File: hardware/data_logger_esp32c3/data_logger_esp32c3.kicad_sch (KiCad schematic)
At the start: 5 parts, among them U1 ESP32-C3-MINI-1

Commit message: remove backups
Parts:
- added J?: USB_C_Receptacle_USB2.0, symbol Connector:USB_C_Receptacle_USB2.0
- added R? (x2): 5.1k, symbol Device:R_Small
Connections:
- net GND: now also J?.A1 (GND), J?.A12 (GND), J?.B1 (GND), J?.B12 (GND), J?.S1 (SHIELD), R?.1, R?.2
- net D-: now reaches U1.26 (GPIO18/USB_D-)
- net D-: now also J?.A7 (D-), J?.B7 (D-)
- net D+: now reaches U1.27 (GPIO19/USB_D+)
- net D+: now also J?.A6 (D+), J?.B6 (D+)
- new net: J?.B5 (CC2), R?.1
- new net: J?.A5 (CC1), R?.2
- new net VBUS: J?.A4 (VBUS), J?.A9 (VBUS), J?.B4 (VBUS), J?.B9 (VBUS)
- no-connect marks 0 -> 2
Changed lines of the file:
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@@
   (junction (at 97.79 114.3) (diameter 0) (color 0 0 0 0)
   )
+  (junction (at 30.48 167.64) (diameter 0) (color 0 0 0 0)
+  )
+  (no_connect (at 53.34 157.48))
+  (no_connect (at 53.34 160.02))
+  (wire (pts (xy 53.34 137.16) (xy 74.93 137.16))
+    (stroke (width 0) (type default) (color 0 0 0 0))
+  )
   (wire (pts (xy 92.71 114.3) (xy 97.79 114.3))
     (stroke (width 0) (type default) (color 0 0 0 0))
   )
+  (wire (pts (xy 53.34 142.24) (xy 53.34 144.78))
+    (stroke (width 0) (type default) (color 0 0 0 0))
+  )
   (wire (pts (xy 92.71 109.22) (xy 102.87 109.22))
     (stroke (width 0) (type default) (color 0 0 0 0))
@@
     (stroke (width 0) (type default) (color 0 0 0 0))
   )
+  (wire (pts (xy 53.34 147.32) (xy 53.34 149.86))
+    (stroke (width 0) (type default) (color 0 0 0 0))
+  )
+  (wire (pts (xy 30.48 167.64) (xy 38.1 167.64))
+    (stroke (width 0) (type default) (color 0 0 0 0))
+  )
+  (wire (pts (xy 53.34 134.62) (xy 82.55 134.62))
+    (stroke (width 0) (type default) (color 0 0 0 0))
+  )
   (wire (pts (xy 102.87 109.22) (xy 107.95 109.22))
     (stroke (width 0) (type default) (color 0 0 0 0))
@@
   (wire (pts (xy 97.79 114.3) (xy 102.87 114.3))
     (stroke (width 0) (type default) (color 0 0 0 0))
+  )
+  (global_label "D-" (shape input) (at 53.34 142.24 0) (fields_autoplaced)
+    (effects (font (size 1.27 1.27)) (justify left))
+    (property "Intersheet References" "${INTERSHEET_REFS}" (id 0) (at 58.5955 142.1606 0)
+      (effects (font (size 1.27 1.27)) (justify left) hide)
+    )
+  )
+  (global_label "D-" (shape input) (at 107.95 88.9 180) (fields_autoplaced)
+    (effects (font (size 1.27 1.27)) (justify right))
+    (property "Intersheet References" "${INTERSHEET_REFS}" (id 0) (at 102.6945 88.9794 0)
+      (effects (font (size 1.27 1.27)) (justify right) hide)
+    )
+  )
+  (global_label "D+" (shape input) (at 107.95 91.44 180) (fields_autoplaced)
+    (effects (font (size 1.27 1.27)) (justify right))
+    (property "Intersheet References" "${INTERSHEET_REFS}" (id 0) (at 102.6945 91.5194 0)
+      (effects (font (size 1.27 1.27)) (justify right) hide)
+    )
+  )
+  (global_label "D+" (shape input) (at 53.34 147.32 0) (fields_autoplaced)
+    (effects (font (size 1.27 1.27)) (justify left))
+    (property "Intersheet References" "${INTERSHEET_REFS}" (id 0) (at 58.5955 147.2406 0)
+      (effects (font (size 1.27 1.27)) (justify left) hide)
+    )
+  )
+  (symbol (lib_id "power:GND") (at 74.93 142.24 0) (unit 1)
+    (in_bom yes) (on_board yes) (fields_autoplaced)
+    (property "Reference" "#PWR?" (id 0) (at 74.93 148.59 0)
+      (effects (font (size 1.27 1.27)) hide)
+    )
+    (property "Value" "GND" (id 1) (at 74.93 147.32 0))
+    (property "Footprint" "" (id 2) (at 74.93 142.24 0)
+      (effects (font (size 1.27 1.27)) hide)
+    )
+    (property "Datasheet" "" (id 3) (at 74.93 142.24 0)
+      (effects (font (size 1.27 1.27)) hide)
+    )
+    (pin "1")
   )
   (symbol (lib_id "power:GND") (at 83.82 58.42 0) (unit 1)
@@
     )
     (property "Datasheet" "" (id 3) (at 83.82 58.42 0)
+      (effects (font (size 1.27 1.27)) hide)
+    )
+    (pin "1")
+  )
+  (symbol (lib_id "Device:R_Small") (at 74.93 139.7 0) (unit 1)
+    (in_bom yes) (on_board yes) (fields_autoplaced)
+    (property "Reference" "R?" (id 0) (at 77.47 138.4299 0)
+      (effects (font (size 1.27 1.27)) (justify left))
+    )
+    (property "Value" "5.1k" (id 1) (at 77.47 140.9699 0)
+      (effects (font (size 1.27 1.27)) (justify left))
+    )
+    (property "Footprint" "" (id 2) (at 74.93 139.7 0)
+      (effects (font (size 1.27 1.27)) hide)
+    )
+    (property "Datasheet" "~" (id 3) (at 74.93 139.7 0)
+      (effects (font (size 1.27 1.27)) hide)
+    )
+    (pin "1")
+    (pin "2")
+  )
+  (symbol (lib_id "Connector:USB_C_Receptacle_USB2.0") (at 38.1 144.78 0) (unit 1)
+    (in_bom yes) (on_board yes) (fields_autoplaced)
+    (property "Reference" "J?" (id 0) (at 38.1 121.92 0))
+    (property "Value" "USB_C_Receptacle_USB2.0" (id 1) (at 38.1 124.46 0))
+    (property "Footprint" "" (id 2) (at 41.91 144.78 0)
+      (effects (font (size 1.27 1.27)) hide)
+    )
+    (property "Datasheet" "https://www.usb.org/sites/default/files/documents/usb_type-c.zip" (id 3) (at 41.91 144.78 0)
+      (effects (font (size 1.27 1.27)) hide)
+    )
+    (pin "A1")
+    (pin "A12")
+    (pin "A4")
+    (pin "A5")
+    (pin "A6")
+    (pin "A7")
+    (pin "A8")
+    (pin "A9")
+    (pin "B1")
+    (pin "B12")
+    (pin "B4")
+    (pin "B5")
+    (pin "B6")
+    (pin "B7")
+    (pin "B8")
+    (pin "B9")
+    (pin "S1")
+  )
+  (symbol (lib_id "power:GND") (at 82.55 139.7 0) (unit 1)
+    (in_bom yes) (on_board yes) (fields_autoplaced)
+    (property "Reference" "#PWR?" (id 0) (at 82.55 146.05 0)
+      (effects (font (size 1.27 1.27)) hide)
+    )
+    (property "Value" "GND" (id 1) (at 82.55 144.78 0))
+    (property "Footprint" "" (id 2) (at 82.55 139.7 0)
+      (effects (font (size 1.27 1.27)) hide)
+    )
+    (property "Datasheet" "" (id 3) (at 82.55 139.7 0)
       (effects (font (size 1.27 1.27)) hide)
     )
@@
     (pin "2")
   )
+  (symbol (lib_id "power:GND") (at 30.48 167.64 0) (unit 1)
+    (in_bom yes) (on_board yes) (fields_autoplaced)
+    (property "Reference" "#PWR?" (id 0) (at 30.48 173.99 0)
+      (effects (font (size 1.27 1.27)) hide)
+    )
+    (property "Value" "GND" (id 1) (at 30.48 172.72 0))
+    (property "Footprint" "" (id 2) (at 30.48 167.64 0)
+      (effects (font (size 1.27 1.27)) hide)
+    )
+    (property "Datasheet" "" (id 3) (at 30.48 167.64 0)
+      (effects (font (size 1.27 1.27)) hide)
+    )
+    (pin "1")
+  )
+  (symbol (lib_id "power:VBUS") (at 53.34 129.54 0) (unit 1)
+    (in_bom yes) (on_board yes) (fields_autoplaced)
+    (property "Reference" "#PWR?" (id 0) (at 53.34 133.35 0)
+      (effects (font (size 1.27 1.27)) hide)
+    )
+    (property "Value" "VBUS" (id 1) (at 53.34 124.46 0))
+    (property "Footprint" "" (id 2) (at 53.34 129.54 0)
+      (effects (font (size 1.27 1.27)) hide)
+    )
+    (property "Datasheet" "" (id 3) (at 53.34 129.54 0)
+      (effects (font (size 1.27 1.27)) hide)
+    )
+    (pin "1")
+  )
+  (symbol (lib_id "Device:R_Small") (at 82.55 137.16 180) (unit 1)
+    (in_bom yes) (on_board yes)
+    (property "Reference" "R?" (id 0) (at 85.09 135.8899 0)
+      (effects (font (size 1.27 1.27)) (justify right))
+    )
+    (property "Value" "5.1k" (id 1) (at 85.09 138.43 0)
+      (effects (font (size 1.27 1.27)) (justify right))
+    )
+    (property "Footprint" "" (id 2) (at 82.55 137.16 0)
+      (effects (font (size 1.27 1.27)) hide)
+    )
+    (property "Datasheet" "~" (id 3) (at 82.55 137.16 0)
+      (effects (font (size 1.27 1.27)) hide)
+    )
+    (pin "1")
+    (pin "2")
+  )
   (sheet_instances
     (path "/" (page "1"))
@@
       (reference "#PWR05") (unit 1) (value "GND") (footprint "")
     )
+    (path "/2152421f-35d0-43cd-896d-06d3fcd0ce30"
+      (reference "#PWR?") (unit 1) (value "GND") (footprint "")
+    )
+    (path "/77e4d49c-766c-4ff2-b941-28c7faeb7c90"
+      (reference "#PWR?") (unit 1) (value "GND") (footprint "")
+    )
+    (path "/e466c578-40f9-47bb-aced-6b9acb8f55cb"
+      (reference "#PWR?") (unit 1) (value "GND") (footprint "")
+    )
+    (path "/eeaa308f-2d5c-4352-8310-d2cc008d34a9"
+      (reference "#PWR?") (unit 1) (value "VBUS") (footprint "")
+    )
     (path "/d5cc3569-1c62-4aa1-9c1d-6a31d547921f"
       (reference "C1") (unit 1) (value "1uF") (footprint "Capacitor_SMD:C_0603_1608Metric")
@@
       (reference "C3") (unit 1) (value "0.1uF") (footprint "Capacitor_SMD:C_0603_1608Metric")
     )
+    (path "/3c576451-e5d6-4069-a440-e981b27fb7a9"
+      (reference "J?") (unit 1) (value "USB_C_Receptacle_USB2.0") (footprint "")
+    )
     (path "/d51cc3ae-b646-440f-9a0d-5b7232e43c54"
       (reference "R1") (unit 1) (value "10k") (footprint "Resistor_SMD:R_0603_1608Metric")
     )
+    (path "/3192ae03-76b6-4acd-8281-ba9fe8edf893"
+      (reference "R?") (unit 1) (value "5.1k") (footprint "")
+    )
+    (path "/f9dc3be0-203f-4f8a-8503-7e1807daf076"
+      (reference "R?") (unit 1) (value "5.1k") (footprint "")
+    )
     (path "/82fb852a-6190-4c86-b807-a06d77b871ca"

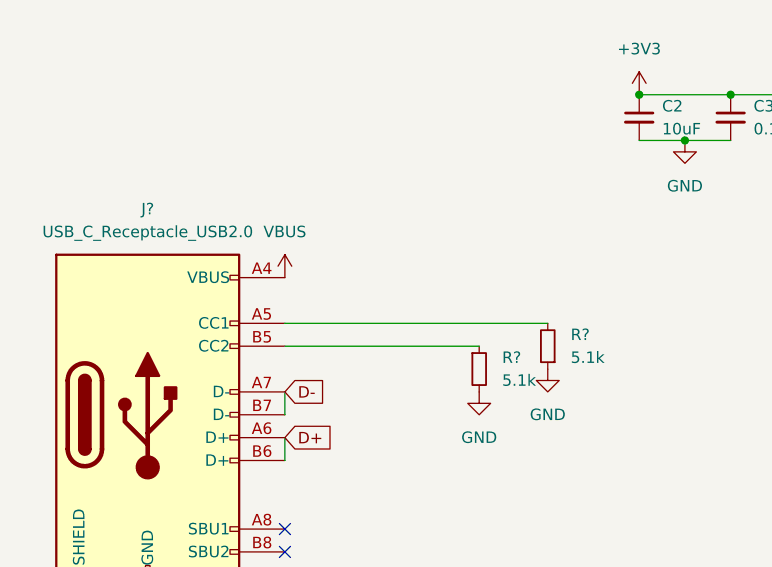
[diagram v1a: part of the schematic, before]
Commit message: add connector
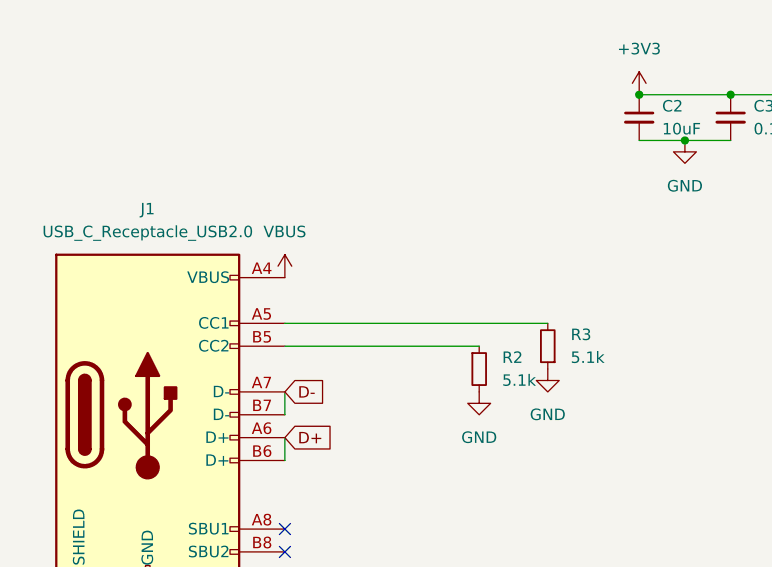
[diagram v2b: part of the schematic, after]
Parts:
- J1: renamed from J?; footprint (none) -> type_c:USB_C_GCT_USB4085
- R2, R3: renamed from R?; footprint (none) -> Resistor_SMD:R_0603_1608Metric
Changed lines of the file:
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@@
   (symbol (lib_id "power:GND") (at 74.93 142.24 0) (unit 1)
     (in_bom yes) (on_board yes) (fields_autoplaced)
-    (property "Reference" "#PWR?" (id 0) (at 74.93 148.59 0)
+    (property "Reference" "#PWR0103" (id 0) (at 74.93 148.59 0)
       (effects (font (size 1.27 1.27)) hide)
     )
@@
   (symbol (lib_id "Device:R_Small") (at 74.93 139.7 0) (unit 1)
     (in_bom yes) (on_board yes) (fields_autoplaced)
-    (property "Reference" "R?" (id 0) (at 77.47 138.4299 0)
+    (property "Reference" "R2" (id 0) (at 77.47 138.4299 0)
       (effects (font (size 1.27 1.27)) (justify left))
     )
@@
       (effects (font (size 1.27 1.27)) (justify left))
     )
-    (property "Footprint" "" (id 2) (at 74.93 139.7 0)
+    (property "Footprint" "Resistor_SMD:R_0603_1608Metric" (id 2) (at 74.93 139.7 0)
       (effects (font (size 1.27 1.27)) hide)
     )
@@
   (symbol (lib_id "Connector:USB_C_Receptacle_USB2.0") (at 38.1 144.78 0) (unit 1)
     (in_bom yes) (on_board yes) (fields_autoplaced)
-    (property "Reference" "J?" (id 0) (at 38.1 121.92 0))
+    (property "Reference" "J1" (id 0) (at 38.1 121.92 0))
     (property "Value" "USB_C_Receptacle_USB2.0" (id 1) (at 38.1 124.46 0))
-    (property "Footprint" "" (id 2) (at 41.91 144.78 0)
+    (property "Footprint" "type_c:USB_C_GCT_USB4085" (id 2) (at 41.91 144.78 0)
       (effects (font (size 1.27 1.27)) hide)
     )
@@
   (symbol (lib_id "power:GND") (at 82.55 139.7 0) (unit 1)
     (in_bom yes) (on_board yes) (fields_autoplaced)
-    (property "Reference" "#PWR?" (id 0) (at 82.55 146.05 0)
+    (property "Reference" "#PWR0102" (id 0) (at 82.55 146.05 0)
       (effects (font (size 1.27 1.27)) hide)
     )
@@
   (symbol (lib_id "power:GND") (at 30.48 167.64 0) (unit 1)
     (in_bom yes) (on_board yes) (fields_autoplaced)
-    (property "Reference" "#PWR?" (id 0) (at 30.48 173.99 0)
+    (property "Reference" "#PWR0101" (id 0) (at 30.48 173.99 0)
       (effects (font (size 1.27 1.27)) hide)
     )
@@
   (symbol (lib_id "power:VBUS") (at 53.34 129.54 0) (unit 1)
     (in_bom yes) (on_board yes) (fields_autoplaced)
-    (property "Reference" "#PWR?" (id 0) (at 53.34 133.35 0)
+    (property "Reference" "#PWR0104" (id 0) (at 53.34 133.35 0)
       (effects (font (size 1.27 1.27)) hide)
     )
@@
   (symbol (lib_id "Device:R_Small") (at 82.55 137.16 180) (unit 1)
     (in_bom yes) (on_board yes)
-    (property "Reference" "R?" (id 0) (at 85.09 135.8899 0)
+    (property "Reference" "R3" (id 0) (at 85.09 135.8899 0)
       (effects (font (size 1.27 1.27)) (justify right))
     )
@@
       (effects (font (size 1.27 1.27)) (justify right))
     )
-    (property "Footprint" "" (id 2) (at 82.55 137.16 0)
+    (property "Footprint" "Resistor_SMD:R_0603_1608Metric" (id 2) (at 82.55 137.16 0)
       (effects (font (size 1.27 1.27)) hide)
     )
@@
       (reference "#PWR05") (unit 1) (value "GND") (footprint "")
     )
+    (path "/e466c578-40f9-47bb-aced-6b9acb8f55cb"
+      (reference "#PWR0101") (unit 1) (value "GND") (footprint "")
+    )
+    (path "/77e4d49c-766c-4ff2-b941-28c7faeb7c90"
+      (reference "#PWR0102") (unit 1) (value "GND") (footprint "")
+    )
     (path "/2152421f-35d0-43cd-896d-06d3fcd0ce30"
-      (reference "#PWR?") (unit 1) (value "GND") (footprint "")
-    )
-    (path "/77e4d49c-766c-4ff2-b941-28c7faeb7c90"
-      (reference "#PWR?") (unit 1) (value "GND") (footprint "")
-    )
-    (path "/e466c578-40f9-47bb-aced-6b9acb8f55cb"
-      (reference "#PWR?") (unit 1) (value "GND") (footprint "")
+      (reference "#PWR0103") (unit 1) (value "GND") (footprint "")
     )
     (path "/eeaa308f-2d5c-4352-8310-d2cc008d34a9"
-      (reference "#PWR?") (unit 1) (value "VBUS") (footprint "")
+      (reference "#PWR0104") (unit 1) (value "VBUS") (footprint "")
     )
     (path "/d5cc3569-1c62-4aa1-9c1d-6a31d547921f"
@@
     )
     (path "/3c576451-e5d6-4069-a440-e981b27fb7a9"
-      (reference "J?") (unit 1) (value "USB_C_Receptacle_USB2.0") (footprint "")
+      (reference "J1") (unit 1) (value "USB_C_Receptacle_USB2.0") (footprint "type_c:USB_C_GCT_USB4085")
     )
     (path "/d51cc3ae-b646-440f-9a0d-5b7232e43c54"
@@
     )
     (path "/3192ae03-76b6-4acd-8281-ba9fe8edf893"
-      (reference "R?") (unit 1) (value "5.1k") (footprint "")
+      (reference "R2") (unit 1) (value "5.1k") (footprint "Resistor_SMD:R_0603_1608Metric")
     )
     (path "/f9dc3be0-203f-4f8a-8503-7e1807daf076"
-      (reference "R?") (unit 1) (value "5.1k") (footprint "")
+      (reference "R3") (unit 1) (value "5.1k") (footprint "Resistor_SMD:R_0603_1608Metric")
     )
     (path "/82fb852a-6190-4c86-b807-a06d77b871ca"
